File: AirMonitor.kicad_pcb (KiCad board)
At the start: 2 copper layers, 49 x 50.4 mm, 60 parts, among them J1 Conn_01x03, J3 USB_C_Receptacle_USB2.0, SW1 RST, SW2 BOOT, U1 WS2812B-2020, U10 AZ1117-3V3, U2 BMP581, U3 SHT45, U4 SCD41, U5 PMS7003, U6 SGP41, U7 5V5, U8 AZ1117-3V3, U9 ESP32-C3-MINI-1

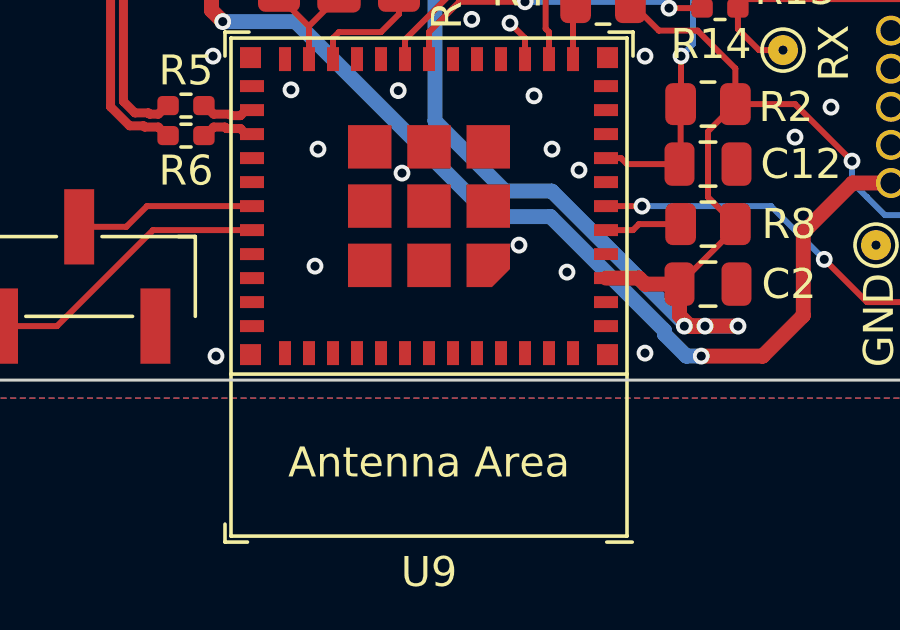
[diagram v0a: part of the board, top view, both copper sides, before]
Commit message: Added JLCPCB mark location
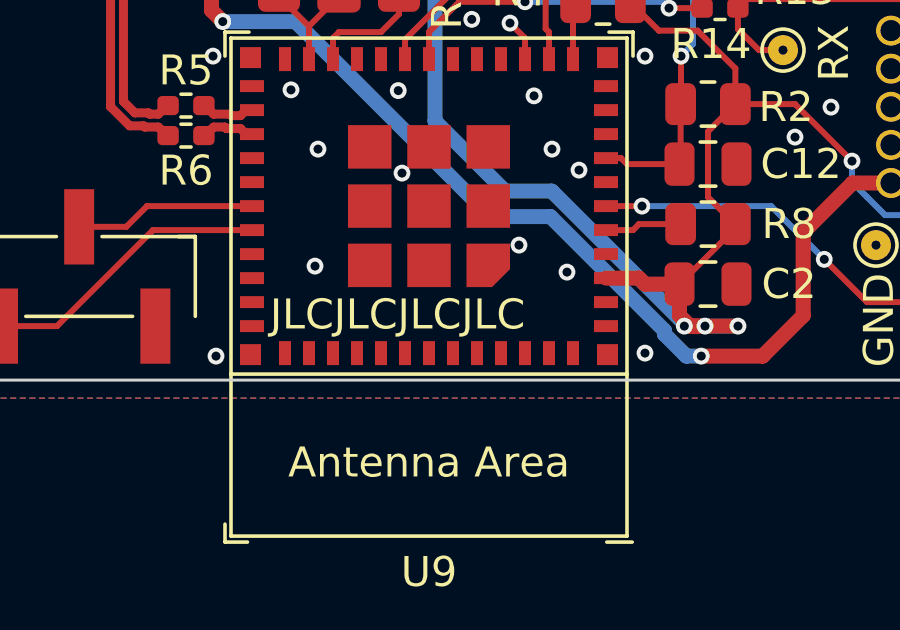
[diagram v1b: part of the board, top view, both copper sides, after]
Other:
- board text added: "JLCJLCJLCJLC"
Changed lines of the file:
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@@
   (setup
     (pad_to_mask_clearance 0)
+    (aux_axis_origin 99 159.4)
     (pcbplotparams
       (layerselection 0x00010fc_ffffffff)
@@
     (effects (font (size 1 1) (thickness 0.15)) (justify left bottom))
   )
+  (gr_text "JLCJLCJLCJLC" (at 120.3 157.8) (layer "F.SilkS")
+    (effects (font (size 1 1) (thickness 0.15)) (justify left bottom))
+  )
